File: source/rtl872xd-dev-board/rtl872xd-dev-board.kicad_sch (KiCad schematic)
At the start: 5 parts, among them J2 Bus_M.2_Socket_B, U1 RTL8722DM

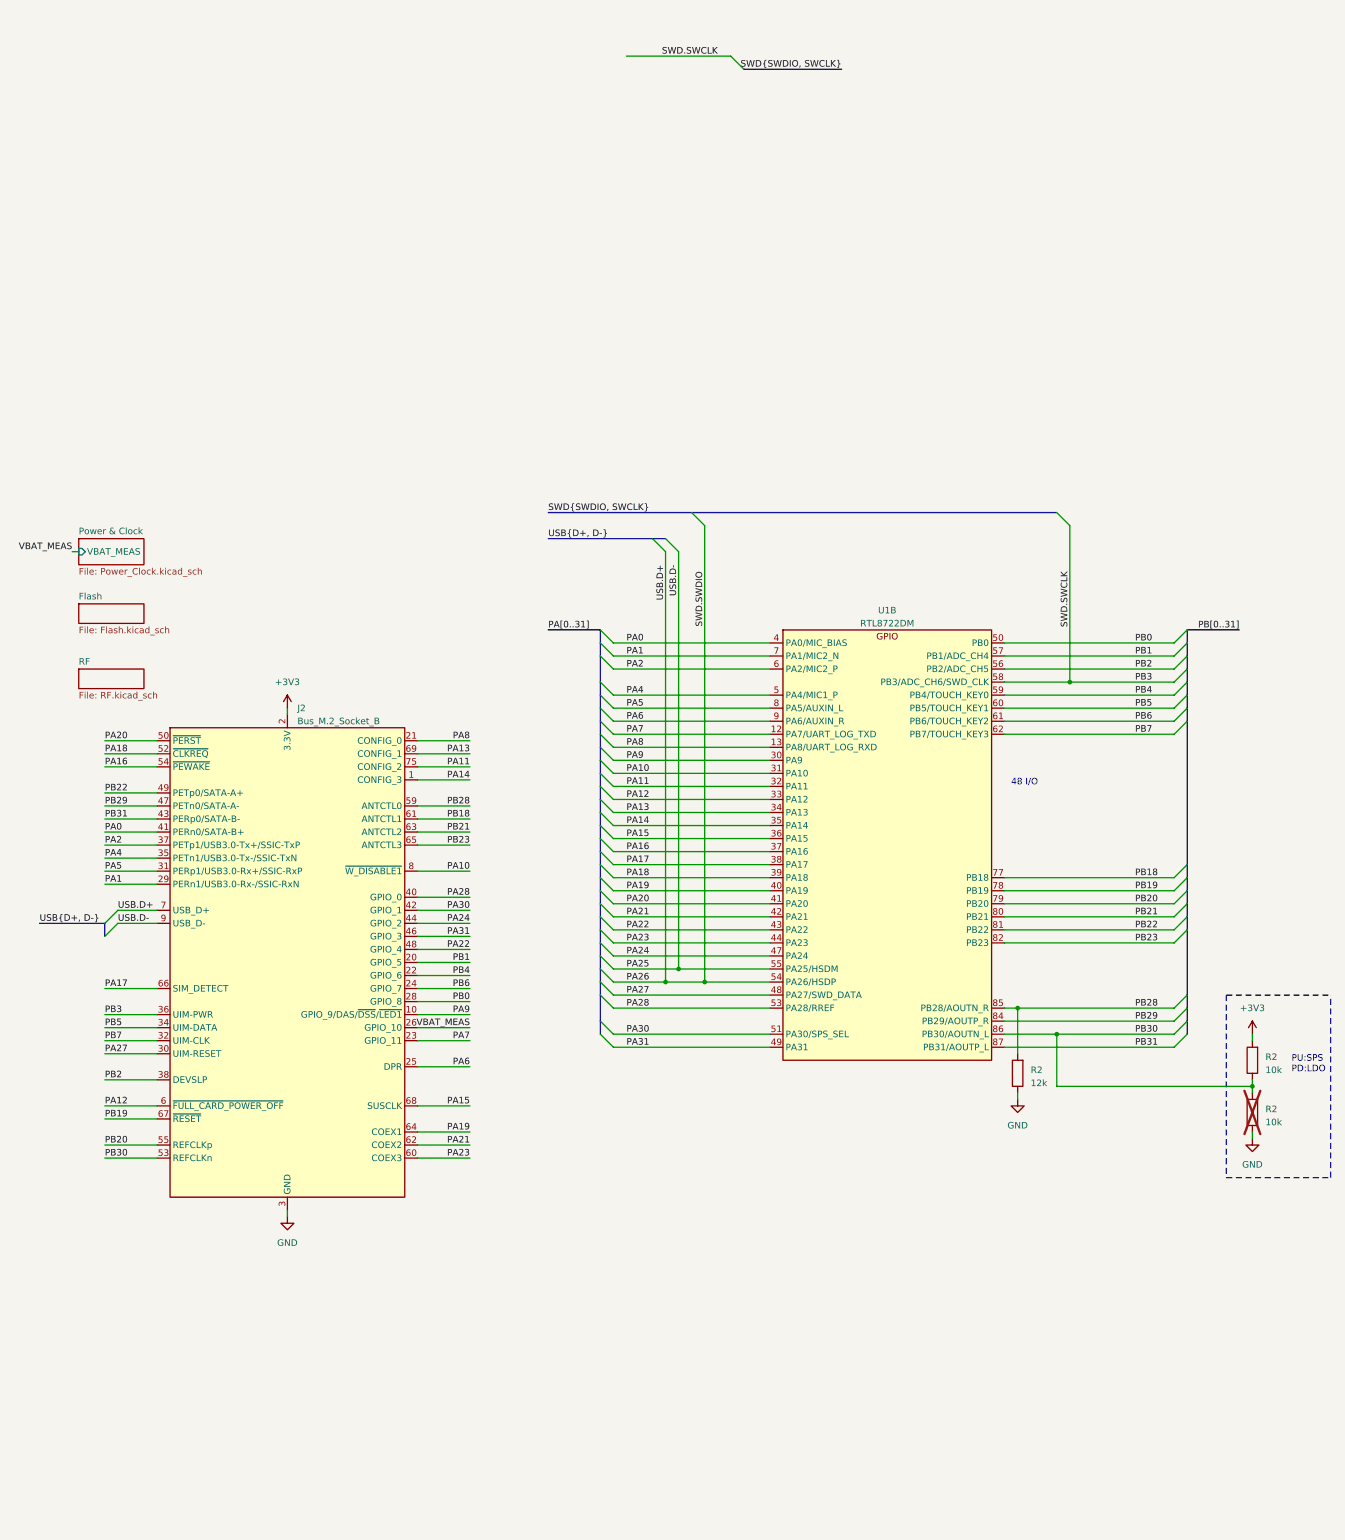
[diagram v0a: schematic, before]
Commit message: added TC2030 debug ports
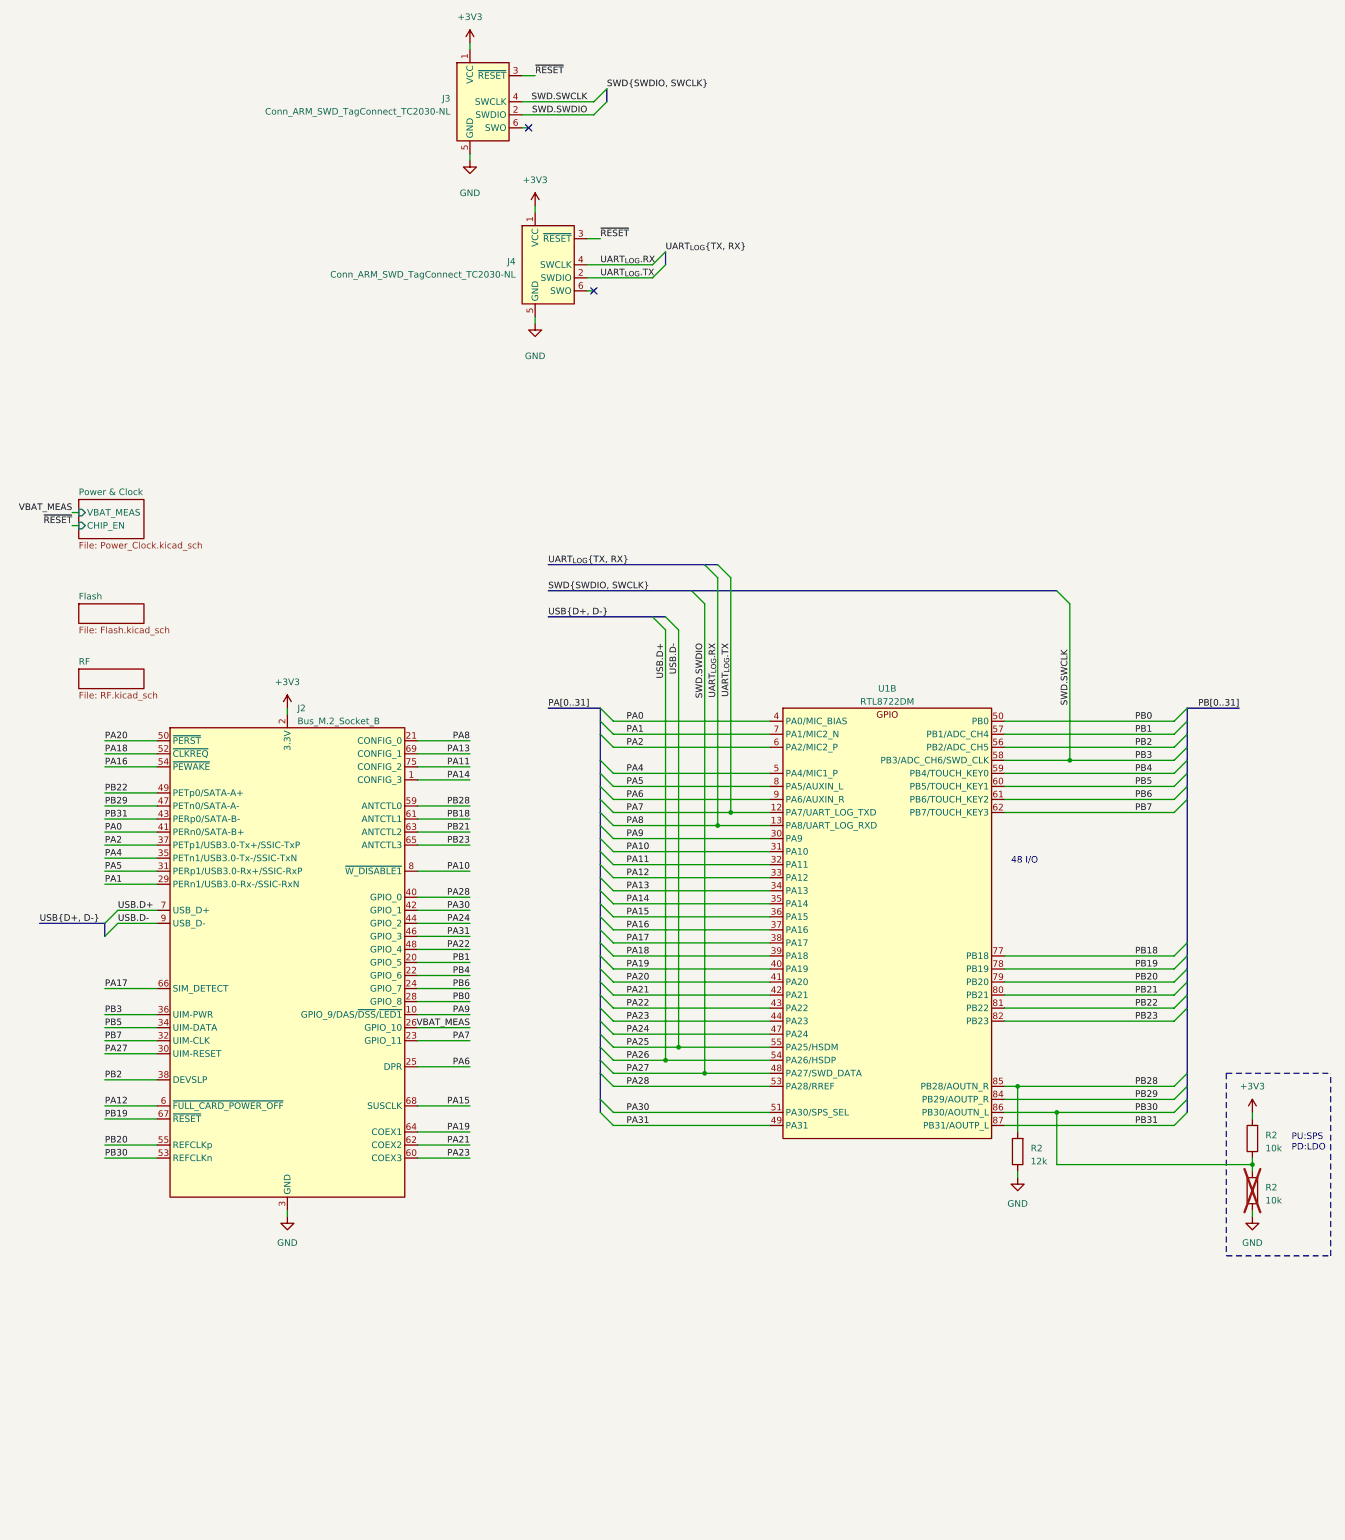
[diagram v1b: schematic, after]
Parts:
- added J3, J4: Conn_ARM_SWD_TagConnect_TC2030-NL, Connector:Tag-Connect_TC2030-IDC-NL_2x03_P1.27mm_Vertical, symbol Connector:Conn_ARM_SWD_TagConnect_TC2030-NL
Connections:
- net +3V3: now also J3.1 (VCC), J4.1 (VCC)
- net GND: now also J3.5 (GND), J4.5 (GND)
- net PA27: now also J3.2 (SWDIO)
- net PA7: now also J4.2 (SWDIO)
- net PA8: now also J4.4 (SWCLK)
- net PB3: now also J3.4 (SWCLK)
- new net ~{RESET}: J3.3 (~{RESET}), J4.3 (~{RESET})
- no-connect marks 0 -> 2
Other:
- sheet Power & Clock ports: added CHIP_EN; removed none
- moved on the sheet: R2, U1B

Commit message: resolve all ERC error, reduce number of warnings
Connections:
- net +3V3 renamed +3.3V

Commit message: tidied up like Marie Kondo
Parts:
- removed J2: Bus_M.2_Socket_B, Connector_M.2:M.2-B-KEY-22x, symbol Connector:Bus_M.2_Socket_B
- removed J3, J4: Conn_ARM_SWD_TagConnect_TC2030-NL, Connector:Tag-Connect_TC2030-IDC-NL_2x03_P1.27mm_Vertical, symbol Connector:Conn_ARM_SWD_TagConnect_TC2030-NL
- R2: now left out of the parts list
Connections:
- no-connect marks 2 -> 0
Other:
- added sheet Debug (Debug.kicad_sch)
- added sheet M.2 (M.2.kicad_sch)
- moved on the sheet: R2, U1B

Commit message: first production version
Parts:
- U1: now left out of the parts list
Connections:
- net PA25 renamed D-
- net PA26 renamed D+
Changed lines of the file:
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@@
   (junction (at 73.66 180.34) (diameter 0) (color 0 0 0 0)
   )
+  (junction (at 76.2 110.49) (diameter 0) (color 0 0 0 0)
+  )
+  (junction (at 73.66 110.49) (diameter 0) (color 0 0 0 0)
+  )
   (junction (at 83.82 134.62) (diameter 0) (color 0 0 0 0)
   )
@@
     (stroke (width 0) (type default))
   )
-  (wire (pts (xy 76.2 93.98) (xy 76.2 177.8))
+  (wire (pts (xy 76.2 110.49) (xy 76.2 177.8))
+    (stroke (width 0) (type default))
+  )
+  (wire (pts (xy 76.2 93.98) (xy 76.2 110.49))
     (stroke (width 0) (type default))
   )
@@
     (stroke (width 0) (type default))
   )
-  (wire (pts (xy 73.66 93.98) (xy 73.66 180.34))
+  (wire (pts (xy 73.66 93.98) (xy 73.66 110.49))
     (stroke (width 0) (type default))
   )
@@
   )
   (wire (pts (xy 17.78 48.26) (xy 17.78 76.2))
+    (stroke (width 0) (type default))
+  )
+  (wire (pts (xy 72.39 110.49) (xy 73.66 110.49))
     (stroke (width 0) (type default))
   )
@@
     (stroke (width 0) (type default))
   )
+  (wire (pts (xy 76.2 110.49) (xy 77.47 110.49))
+    (stroke (width 0) (type default))
+  )
   (wire (pts (xy 63.5 134.62) (xy 83.82 134.62))
     (stroke (width 0) (type default))
@@
     (stroke (width 0) (type default))
   )
+  (wire (pts (xy 73.66 110.49) (xy 73.66 180.34))
+    (stroke (width 0) (type default))
+  )
   (bus (pts (xy 60.96 134.62) (xy 60.96 132.08))
     (stroke (width 0) (type default))
@@
   (label "PA1" (at 66.04 116.84 0) (fields_autoplaced)
     (effects (font (size 1.27 1.27)) (justify left bottom))
+  )
+  (global_label "D+" (shape input) (at 72.39 110.49 180) (fields_autoplaced)
+    (effects (font (size 1.27 1.27)) (justify right))
+    (property "Intersheetrefs" "${INTERSHEET_REFS}" (at 66.6418 110.49 0)
+      (effects (font (size 1.27 1.27)) (justify right) hide)
+    )
+  )
+  (global_label "D-" (shape input) (at 77.47 110.49 0) (fields_autoplaced)
+    (effects (font (size 1.27 1.27)) (justify left))
+    (property "Intersheetrefs" "${INTERSHEET_REFS}" (at 83.2182 110.49 0)
+      (effects (font (size 1.27 1.27)) (justify left) hide)
+    )
   )
   (symbol (lib_id "power:+3.3V") (at 160.02 190.5 0) (unit 1)
@@
   )
   (symbol (lib_id "MCU_Realtek:RTL8722DM") (at 111.76 167.64 0) (unit 2)
-    (in_bom yes) (on_board yes) (dnp no) (fields_autoplaced)
+    (in_bom no) (on_board yes) (dnp no) (fields_autoplaced)
     (property "Reference" "U1" (at 111.76 107.95 0)
       (effects (font (size 1.27 1.27)))
